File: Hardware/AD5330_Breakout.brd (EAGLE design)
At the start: 20.3 x 27.9 mm, 9 parts, among them U1 AD5330

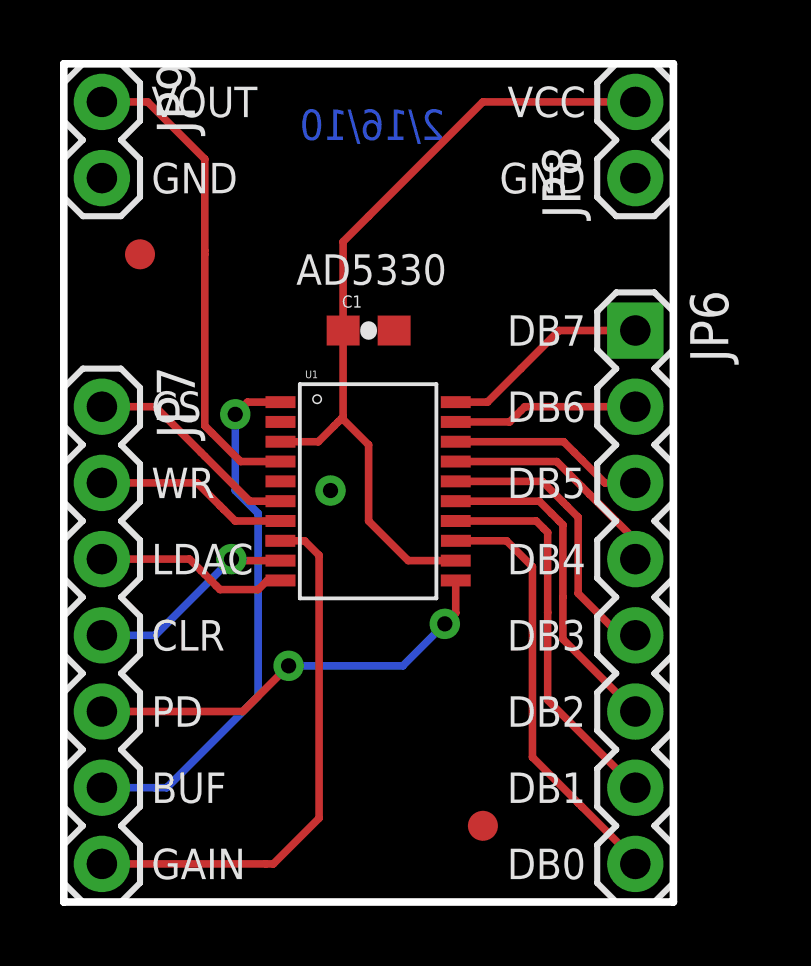
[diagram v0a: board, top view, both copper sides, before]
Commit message: Revision changes
-Cleaned up schematic
-Added OSHW Logo
-0402->0603
-Added 10uf cap for filtration off of VDD as per the datasheet
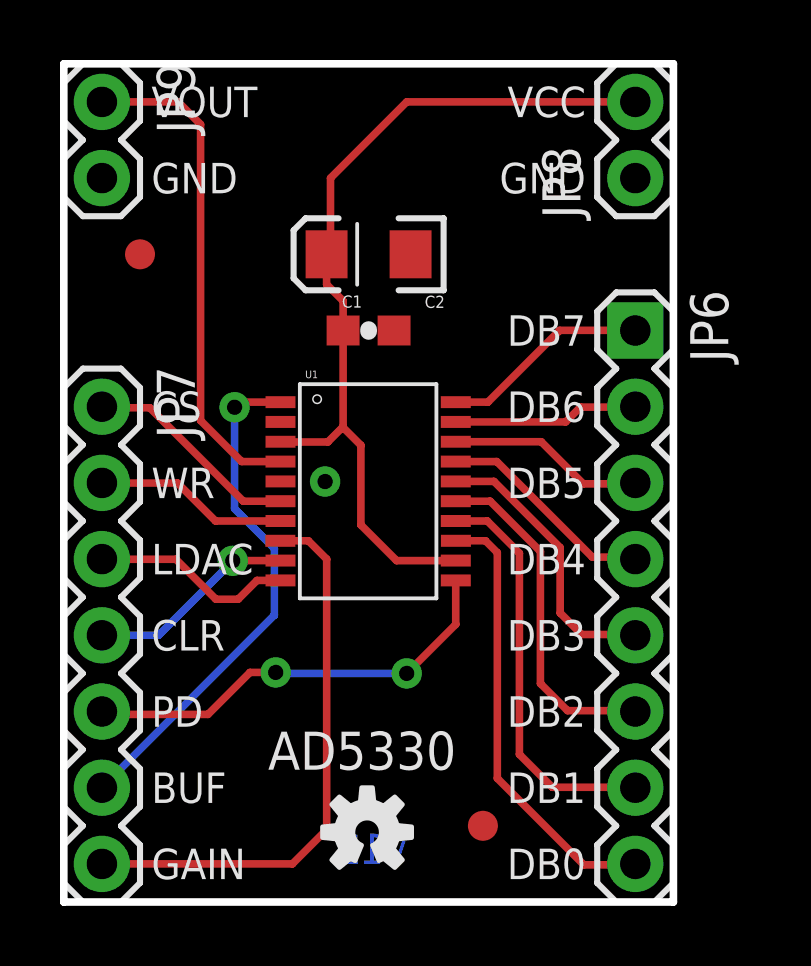
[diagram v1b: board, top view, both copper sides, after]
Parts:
- added C2: 10uF, SparkFun-Capacitors:EIA3216
- added FRAME1: FRAME-LETTER, SparkFun-Aesthetics:CREATIVE_COMMONS
- added LOGO1: OSHW-LOGOS, SparkFun-Aesthetics:OSHW-LOGO-S
- C1: device SparkFun:0603-CAP -> SparkFun-Capacitors:0603-CAP
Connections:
- net GND: now also C2.C
- net VCC: now also C2.A
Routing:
- net VCC: track 27.2 -> 29.3 mm
- net GAIN: track 18.1 -> 18.8 mm
- net DB1: track 12.9 -> 13.6 mm
- net DB0: track 14.2 -> 14.9 mm
- net BUF: track 17.9 -> 17.2 mm
- net VOUT: track 16.1 -> 16.7 mm
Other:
- board text added: "v12"
- board text removed: "2/16/10"
